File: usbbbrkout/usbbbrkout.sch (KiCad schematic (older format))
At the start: 6 parts, among them P101 CONN_01X01, P102 CONN_01X01, P103 CONN_01X01, P104 CONN_01X01, P105 USB_B

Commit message: Switch designs to the 4.0.7 symbol and footprint library.
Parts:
- P105: symbol USB_B-RESCUE-usbbbrkout -> USB_B
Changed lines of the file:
@@
 EESchema Schematic File Version 2
-LIBS:usbbbrkout-rescue
 LIBS:local
 LIBS:power
@@
 	5000 4400 5000 4500
 $Comp
-L USB_B-RESCUE-usbbbrkout P105
+L USB_B P105
 U 1 1 5ADFC07A
 P 6000 3400

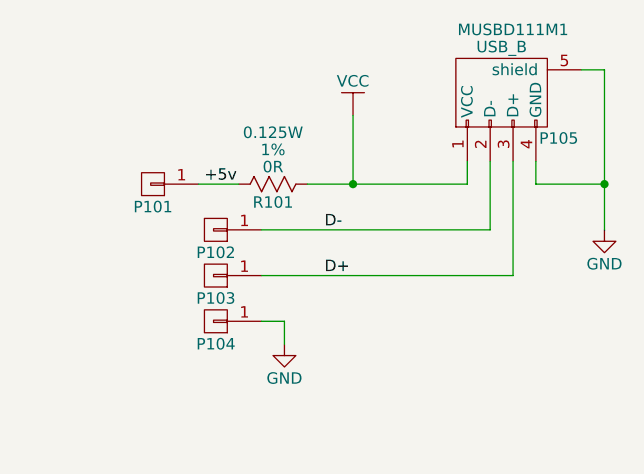
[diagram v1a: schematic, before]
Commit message: Cleanup update to breakout boards. Upload to OSHpark.
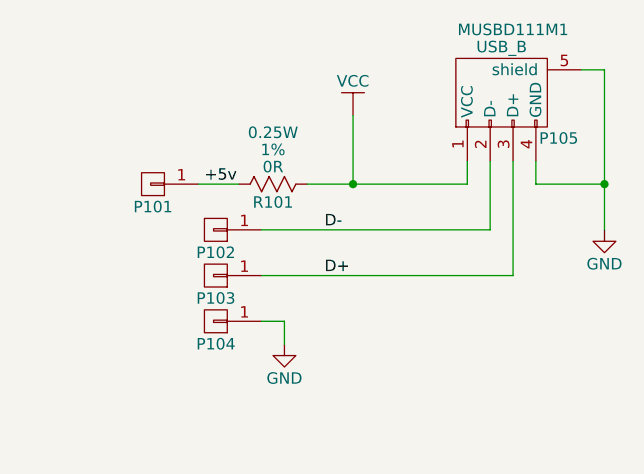
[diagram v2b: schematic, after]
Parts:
- R101: Power 0.125W -> 0.25W
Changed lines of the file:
@@
 F 3 "" V 5030 3800 30  0000 C CNN
 F 4 "1%" V 4800 3800 50  0000 C CNN "Tolerance"
-F 5 "0.125W" V 4725 3800 50  0000 C CNN "Power"
+F 5 "0.25W" V 4725 3800 50  0000 C CNN "Power"
 F 6 "Vishay Dale" V 5100 3800 50  0001 C CNN "Manufacturer"
 F 7 "CRCW12060000Z0EA" V 5175 3800 50  0001 C CNN "PartNum"

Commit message: Adjust clearances of ground and vcc pours.
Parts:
- R101: footprint local:C_1206_HandSoldering -> local:R_1206_HandSoldering
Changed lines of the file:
@@
 F 0 "R101" V 5030 3800 50  0000 C CNN
 F 1 "0R" V 4875 3800 50  0000 C CNN
-F 2 "local:C_1206_HandSoldering" V 4880 3800 30  0001 C CNN
+F 2 "local:R_1206_HandSoldering" V 4880 3800 30  0001 C CNN
 F 3 "" V 5030 3800 30  0000 C CNN
 F 4 "1%" V 4800 3800 50  0000 C CNN "Tolerance"

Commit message: Update USB-B breakout board to kicad 5.1. Regenerate output files.
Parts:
- P101, P102, P103, P104: symbol CONN_01X01 -> conn:CONN_01X01
- P105: symbol USB_B -> Local:USB_B
- R101: symbol R_local -> Local:R_local
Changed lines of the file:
@@
-EESchema Schematic File Version 2
-LIBS:local
-LIBS:power
-LIBS:device
-LIBS:transistors
-LIBS:conn
-LIBS:linear
-LIBS:regul
-LIBS:74xx
-LIBS:cmos4000
-LIBS:adc-dac
-LIBS:memory
-LIBS:xilinx
-LIBS:microcontrollers
-LIBS:dsp
-LIBS:microchip
-LIBS:analog_switches
-LIBS:motorola
-LIBS:texas
-LIBS:intel
-LIBS:audio
-LIBS:interface
-LIBS:digital-audio
-LIBS:philips
-LIBS:display
-LIBS:cypress
-LIBS:siliconi
-LIBS:opto
-LIBS:atmel
-LIBS:contrib
-LIBS:valves
-LIBS:usbbbrkout-cache
-EELAYER 25 0
+EESchema Schematic File Version 4
+EELAYER 30 0
 EELAYER END
 $Descr A4 11693 8268
@@
 $EndDescr
 $Comp
-L CONN_01X01 P102
+L conn:CONN_01X01 P102
 U 1 1 5AD927DD
 P 4700 4000
@@
 $EndComp
 $Comp
-L CONN_01X01 P103
+L conn:CONN_01X01 P103
 U 1 1 5AD928A6
 P 4700 4200
@@
 $EndComp
 $Comp
-L GND #PWR01
+L power:GND #PWR01
 U 1 1 5AD92B85
 P 6400 4000
@@
 	6300 3300 6400 3300
 Wire Wire Line
-	6400 3300 6400 4000
+	6400 3300 6400 3800
 Wire Wire Line
 	4900 4200 6000 4200
@@
 	4625 3800 4800 3800
 Wire Wire Line
-	5100 3800 5800 3800
+	5100 3800 5300 3800
 Wire Wire Line
 	5300 3800 5300 3500
 $Comp
-L VCC #PWR02
+L Local:VCC #PWR02
 U 1 1 5ADE9D9C
 P 5300 3500
@@
 $EndComp
 $Comp
-L CONN_01X01 P101
+L conn:CONN_01X01 P101
 U 1 1 5ADEA025
 P 4425 3800
@@
 $EndComp
 $Comp
-L CONN_01X01 P104
+L conn:CONN_01X01 P104
 U 1 1 5ADEA065
 P 4700 4400
@@
 Connection ~ 5300 3800
 $Comp
-L GND #PWR03
+L power:GND #PWR03
 U 1 1 5ADEA436
 P 5000 4500
@@
 	5000 4400 5000 4500
 $Comp
-L USB_B P105
+L Local:USB_B P105
 U 1 1 5ADFC07A
 P 6000 3400
@@
 $EndComp
 $Comp
-L R_local R101
+L Local:R_local R101
 U 1 1 5AE28356
 P 4950 3800
@@
 Text Label 4650 3800 0    50   ~ 0
 +5v
+Wire Wire Line
+	6400 3800 6400 4000
+Wire Wire Line
+	5300 3800 5800 3800
 $EndSCHEMATC

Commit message: Fix rj45 break out board to point to 5.1 symbol libraries. Fix USB-A break out board to point to 5.1 symbol libraries. Fix USB-B break out board to point to 5.1 symbol libraries.
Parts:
- P101, P102, P103, P104: symbol conn:CONN_01X01 -> Connector_Generic:Conn_01x01
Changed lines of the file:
@@
 $EndDescr
 $Comp
-L conn:CONN_01X01 P102
+L Connector_Generic:Conn_01x01 P102
 U 1 1 5AD927DD
 P 4700 4000
@@
 $EndComp
 $Comp
-L conn:CONN_01X01 P103
+L Connector_Generic:Conn_01x01 P103
 U 1 1 5AD928A6
 P 4700 4200
@@
 $EndComp
 $Comp
-L conn:CONN_01X01 P101
+L Connector_Generic:Conn_01x01 P101
 U 1 1 5ADEA025
 P 4425 3800
@@
 $EndComp
 $Comp
-L conn:CONN_01X01 P104
+L Connector_Generic:Conn_01x01 P104
 U 1 1 5ADEA065
 P 4700 4400
